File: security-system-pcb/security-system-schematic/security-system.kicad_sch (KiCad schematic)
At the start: 9 parts, among them J1 Conn_01x06_Pin, J2 USB_C_Receptacle_USB2.0_16P

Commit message: Add PCB changes
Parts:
- D1, D2: footprint (none) -> LED_THT:LED_D5.0mm
- J1: footprint (none) -> Connector_Molex:Molex_PicoBlade_53047-0610_1x06_P1.25mm_Vertical
- J2: footprint (none) -> Connector_USB:USB_C_Receptacle_GCT_USB4105-xx-A_16P_TopMnt_Horizontal
- R1: value 120 kΩ -> 120 Ω; footprint (none) -> Resistor_THT:R_Axial_DIN0207_L6.3mm_D2.5mm_P7.62mm_Horizontal
- R2, R3, R4: footprint (none) -> Resistor_THT:R_Axial_DIN0207_L6.3mm_D2.5mm_P7.62mm_Horizontal
- U1: value ~ -> ESP32-Header; footprint (none) -> security-system-footprints:esp32-header
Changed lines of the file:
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@@
 			)
 		)
-		(property "Footprint" ""
+		(property "Footprint" "Resistor_THT:R_Axial_DIN0207_L6.3mm_D2.5mm_P7.62mm_Horizontal"
 			(at 81.28 95.758 90)
 			(effects
@@
 			)
 		)
-		(property "Footprint" ""
+		(property "Footprint" "LED_THT:LED_D5.0mm"
 			(at 251.46 109.22 0)
 			(effects
@@
 			)
 		)
-		(property "Footprint" ""
+		(property "Footprint" "Connector_USB:USB_C_Receptacle_GCT_USB4105-xx-A_16P_TopMnt_Horizontal"
 			(at 59.69 101.6 0)
 			(effects
@@
 			)
 		)
-		(property "Footprint" ""
+		(property "Footprint" "LED_THT:LED_D5.0mm"
 			(at 219.71 109.22 0)
 			(effects
@@
 		(on_board yes)
 		(dnp no)
+		(fields_autoplaced yes)
 		(property "Reference" "U1"
-			(at 184.15 71.12 0)
-			(effects
-				(font
-					(size 1.27 1.27)
-				)
-			)
-		)
-		(property "Value" "~"
 			(at 184.15 73.66 0)
 			(effects
@@
 					(size 1.27 1.27)
 				)
-				(hide yes)
-			)
-		)
-		(property "Footprint" ""
+			)
+		)
+		(property "Value" "ESP32-Header"
+			(at 184.15 73.66 0)
+			(effects
+				(font
+					(size 1.27 1.27)
+				)
+				(hide yes)
+			)
+		)
+		(property "Footprint" "security-system-footprints:esp32-header"
 			(at 184.15 88.9 0)
 			(effects
@@
 			)
 		)
-		(property "Footprint" ""
+		(property "Footprint" "Resistor_THT:R_Axial_DIN0207_L6.3mm_D2.5mm_P7.62mm_Horizontal"
 			(at 81.28 93.218 90)
 			(effects
@@
 			)
 		)
-		(property "Footprint" ""
+		(property "Footprint" "Resistor_THT:R_Axial_DIN0207_L6.3mm_D2.5mm_P7.62mm_Horizontal"
 			(at 249.682 92.71 90)
 			(effects
@@
 			)
 		)
-		(property "Footprint" ""
+		(property "Footprint" "Connector_Molex:Molex_PicoBlade_53047-0610_1x06_P1.25mm_Vertical"
 			(at 128.27 102.87 0)
 			(effects
@@
 			)
 		)
-		(property "Value" "120 kΩ"
+		(property "Value" "120 Ω"
 			(at 222.25 93.9799 0)
 			(effects
@@
 			)
 		)
-		(property "Footprint" ""
+		(property "Footprint" "Resistor_THT:R_Axial_DIN0207_L6.3mm_D2.5mm_P7.62mm_Horizontal"
 			(at 217.932 92.71 90)
 			(effects

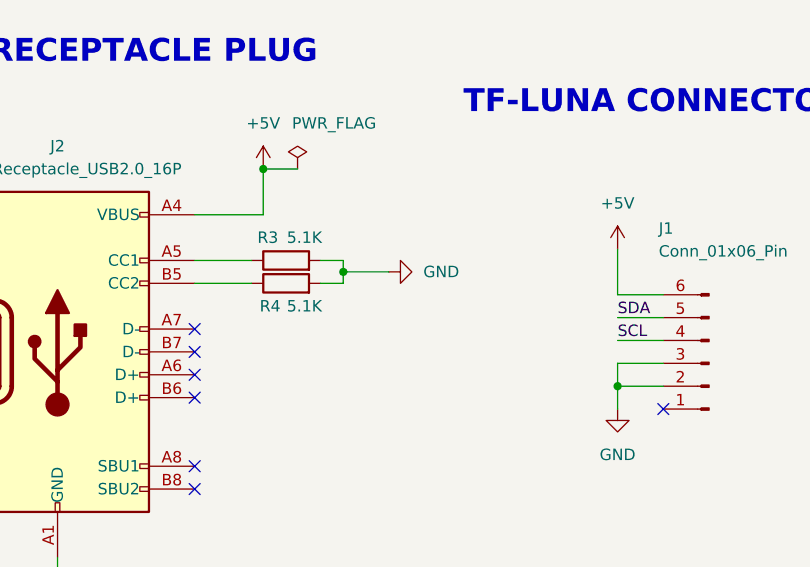
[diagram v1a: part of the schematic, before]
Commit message: Add PCB changes and 3D case
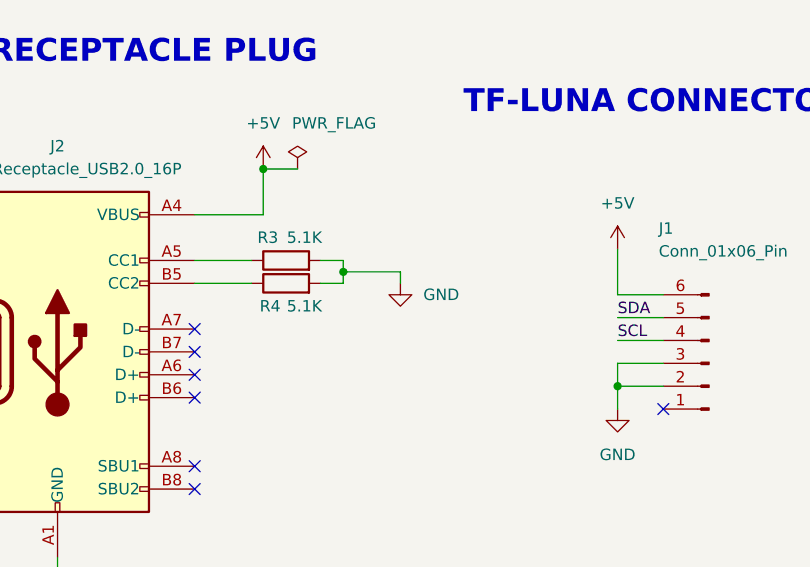
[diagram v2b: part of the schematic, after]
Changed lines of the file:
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@@
+	)
+	(junction
+		(at 166.37 80.01)
+		(diameter 0)
+		(color 0 0 0 0)
+	)
+	(junction
+		(at 78.74 81.28)
+		(diameter 0)
+		(color 0 0 0 0)
 	)
 	(junction
@@
 		(color 0 0 0 0)
 	)
-	(junction
-		(at 166.37 80.01)
-		(diameter 0)
-		(color 0 0 0 0)
-	)
-	(junction
-		(at 78.74 81.28)
-		(diameter 0)
-		(color 0 0 0 0)
-	)
 	(no_connect
 		(at 71.12 101.6)
@@
 	(wire
 		(pts
-			(xy 87.63 93.98) (xy 87.63 92.71)
-		)
-		(stroke
-			(width 0)
-			(type default)
-		)
-	)
-	(wire
-		(pts
 			(xy 251.46 96.52) (xy 251.46 105.41)
 		)
@@
 	(wire
 		(pts
+			(xy 87.63 92.71) (xy 87.63 93.98)
+		)
+		(stroke
+			(width 0)
+			(type default)
+		)
+	)
+	(wire
+		(pts
 			(xy 85.09 93.98) (xy 87.63 93.98)
 		)
@@
 	(wire
 		(pts
-			(xy 92.71 92.71) (xy 87.63 92.71)
+			(xy 93.98 92.71) (xy 87.63 92.71)
+		)
+		(stroke
+			(width 0)
+			(type default)
+		)
+	)
+	(wire
+		(pts
+			(xy 93.98 92.71) (xy 93.98 93.98)
 		)
 		(stroke
@@
 	(symbol
 		(lib_id "power:GND")
-		(at 92.71 92.71 90)
+		(at 93.98 93.98 0)
 		(unit 1)
 		(exclude_from_sim no)
@@
 		(fields_autoplaced yes)
 		(property "Reference" "#PWR03"
-			(at 99.06 92.71 0)
+			(at 93.98 100.33 0)
 			(effects
 				(font
@@
 		)
 		(property "Value" "GND"
-			(at 96.52 92.7099 90)
-			(effects
-				(font
-					(size 1.27 1.27)
-				)
-				(justify right)
+			(at 96.52 95.2499 0)
+			(effects
+				(font
+					(size 1.27 1.27)
+				)
+				(justify left)
 			)
 		)
 		(property "Footprint" ""
-			(at 92.71 92.71 0)
+			(at 93.98 93.98 0)
 			(effects
 				(font
@@
 		)
 		(property "Datasheet" ""
-			(at 92.71 92.71 0)
+			(at 93.98 93.98 0)
 			(effects
 				(font
@@
 		)
 		(property "Description" "Power symbol creates a global label with name \"GND\" , ground"
-			(at 92.71 92.71 0)
-			(effects
-				(font
+			(at 93.98 93.98 0)
+			(effects
+				(font

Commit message: Push PCB version 1.3
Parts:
- R2: value 150 Ω -> 60 Ω
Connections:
- net +5V: no longer R2.1
- net LED_STATUS: now reaches U1.5 (GPIO4)
- net LED_STATUS: now also R2.1
- no-connect marks 42 -> 41
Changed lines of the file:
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@@
 	(text "RED LED"
 		(exclude_from_sim no)
-		(at 251.46 68.834 0)
+		(at 254.762 68.834 0)
 		(effects
 			(font
@@
 	)
 	(no_connect
-		(at 171.45 88.9)
-	)
-	(no_connect
 		(at 171.45 114.3)
 	)
@@
 	(wire
 		(pts
+			(xy 251.46 83.82) (xy 262.89 83.82)
+		)
+		(stroke
+			(width 0)
+			(type default)
+		)
+	)
+	(wire
+		(pts
 			(xy 85.09 93.98) (xy 87.63 93.98)
 		)
@@
 	(wire
 		(pts
+			(xy 158.75 88.9) (xy 171.45 88.9)
+		)
+		(stroke
+			(width 0)
+			(type default)
+		)
+	)
+	(wire
+		(pts
 			(xy 118.11 105.41) (xy 123.19 105.41)
 		)
@@
 			(width 0)
 			(type default)
+		)
+	)
+	(label "LED_STATUS"
+		(at 251.46 83.82 0)
+		(effects
+			(font
+				(size 1.27 1.27)
+			)
+			(justify left bottom)
 		)
 	)
@@
 	(label "SCL"
 		(at 166.37 116.84 0)
+		(effects
+			(font
+				(size 1.27 1.27)
+			)
+			(justify left bottom)
+		)
+	)
+	(label "LED_STATUS"
+		(at 158.75 88.9 0)
 		(effects
 			(font
@@
 			)
 		)
-		(property "Value" "150 Ω"
+		(property "Value" "60 Ω"
 			(at 254 93.9799 0)
 			(effects
@@
 					(unit 1)
 				)
-			)
-		)
-	)
-	(symbol
-		(lib_id "power:+5V")
-		(at 251.46 83.82 0)
-		(unit 1)
-		(exclude_from_sim no)
-		(in_bom yes)
-		(on_board yes)
-		(dnp no)
-		(fields_autoplaced yes)
-		(property "Reference" "#PWR010"
-			(at 251.46 87.63 0)
-			(effects
-				(font
-					(size 1.27 1.27)
-				)
-				(hide yes)
-			)
-		)
-		(property "Value" "+5V"
-			(at 251.46 78.74 0)
-			(effects
-				(font
-					(size 1.27 1.27)
-				)
-			)
-		)
-		(property "Footprint" ""
-			(at 251.46 83.82 0)
-			(effects
-				(font
-					(size 1.27 1.27)
-				)
-				(hide yes)
-			)
-		)
-		(property "Datasheet" ""
-			(at 251.46 83.82 0)
-			(effects
-				(font
-					(size 1.27 1.27)
-				)
-				(hide yes)
-			)
-		)
-		(property "Description" "Power symbol creates a global label with name \"+5V\""
-			(at 251.46 83.82 0)
-			(effects
-				(font
-					(size 1.27 1.27)
-				)
-				(hide yes)
-			)
-		)
-		(pin "1"
-		)
-		(instances
-			(project ""
-				(path "/3266c3d5-665e-4488-8076-23363c237f18"
-					(reference "#PWR010")
-					(unit 1)
-				)
